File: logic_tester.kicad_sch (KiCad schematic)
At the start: 20 parts, among them U1 LM339D

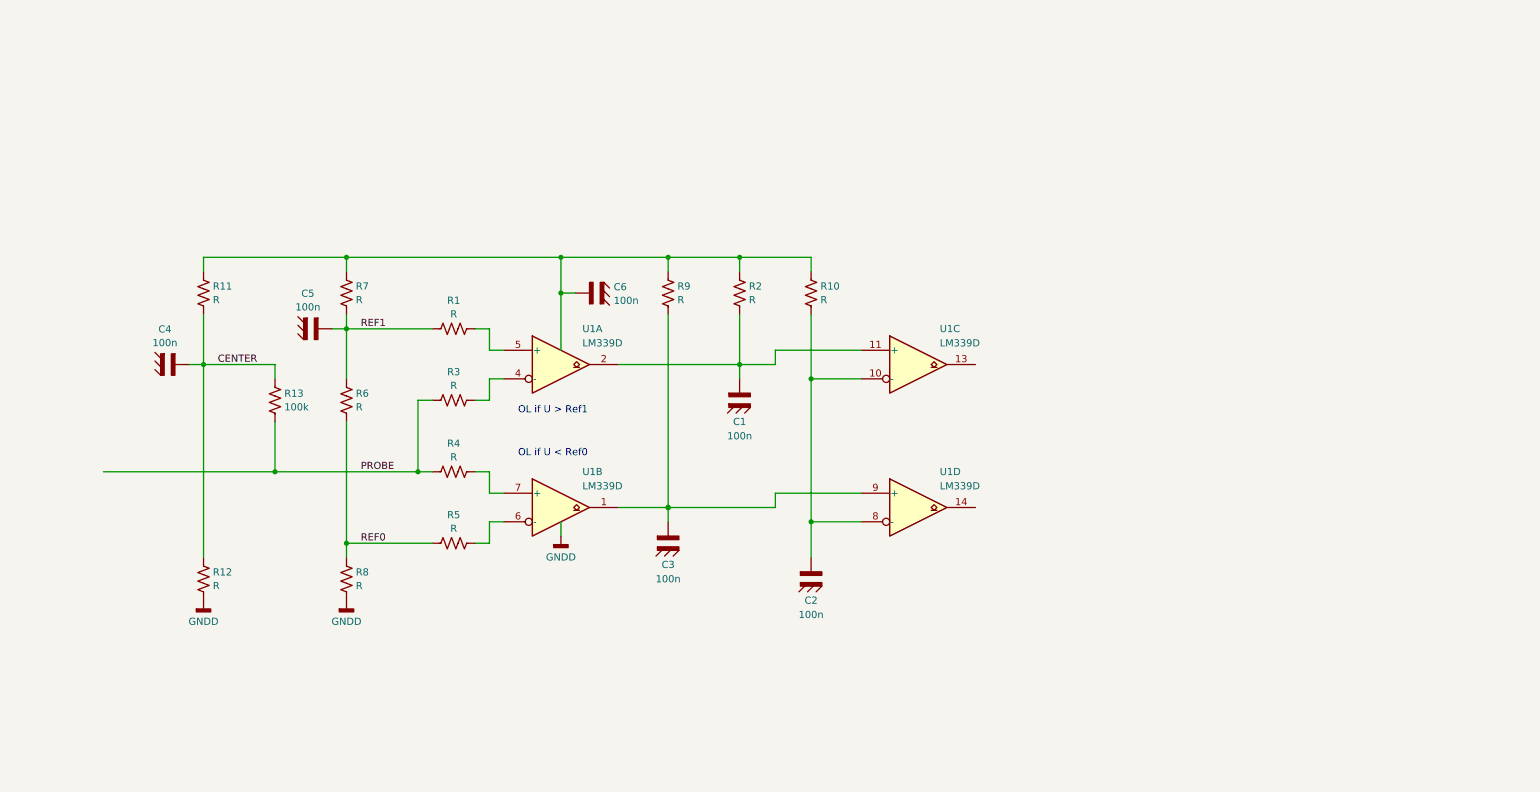
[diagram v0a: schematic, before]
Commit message: Leds with direct supply - bad idea
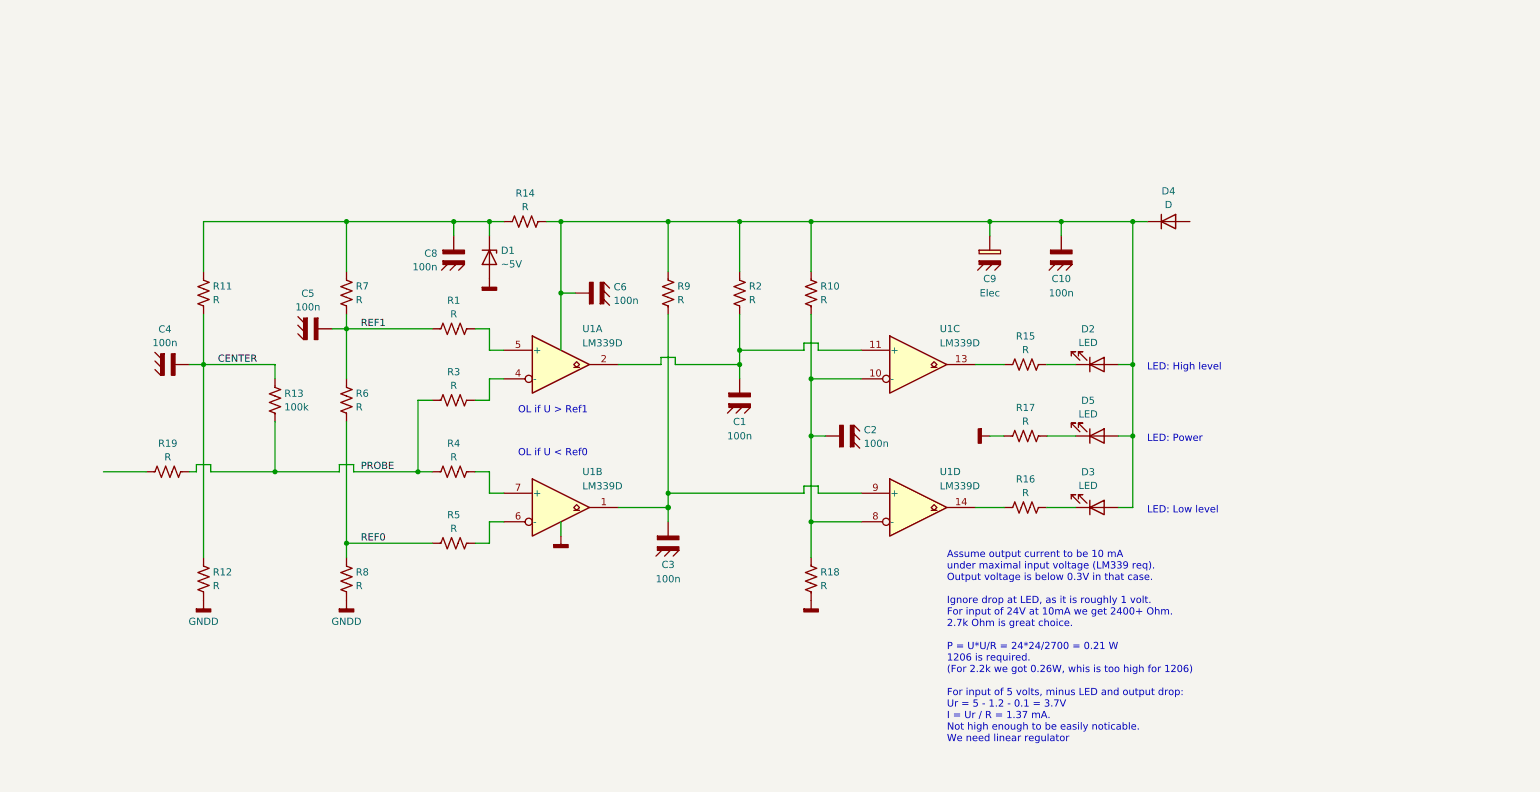
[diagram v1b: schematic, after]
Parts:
- added C10, C8: 100n, symbol symbol:C_GND
- added C9: Elec, symbol symbol:CP_GND
- added D1: ~5V, symbol Device:D_Zener
- added D2, D3, D5: LED, symbol Device:LED
- added D4: D, symbol Device:D
- added R14, R15, R16, R17, R18, R19: R, symbol symbol:R
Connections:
- net GNDD: now also C10.2 (GNDD), C8.2 (GNDD), C9.2 (GNDD), D1.2 (A), R17.1, R18.2
- net PROBE: now also R19.2
- net V+: now also C10.1, C9.1, D2.2 (A), D3.2 (A), D4.1 (K), D5.2 (A), R14.2; no longer R11.1, R7.1
- net at C2.1, R10.2, U1.10 (-)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: now also R18.1
- net at U1.14: now also R16.1
- net at U1.13: now also R15.1
- new net: D5.1 (K), R17.2
- new net: D2.1 (K), R15.2
- new net: D3.1 (K), R16.2
- new net: C8.1, D1.1 (K), R11.1, R14.1, R7.1
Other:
- note added: "Assume output current to be 10 mA under maximal input voltage (LM339 req). Output voltage is below 0.3V in that case. Ignore drop at LED, as it is roughly 1 volt. For input of 24V at 10mA we get 2400+ Ohm. 2.7k Ohm is great choice. P = U*U/R = 24*24/2700 = 0.21 W 1206 is required. (For 2.2k we got 0.26W, whis is too high for 1206) For input of 5 volts, minus LED and output drop: Ur = 5 - 1.2 - 0.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"
- note added: "LED: High level"
- note added: "LED: Low level"
- note added: "LED: Power"

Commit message: Voltage regulator added
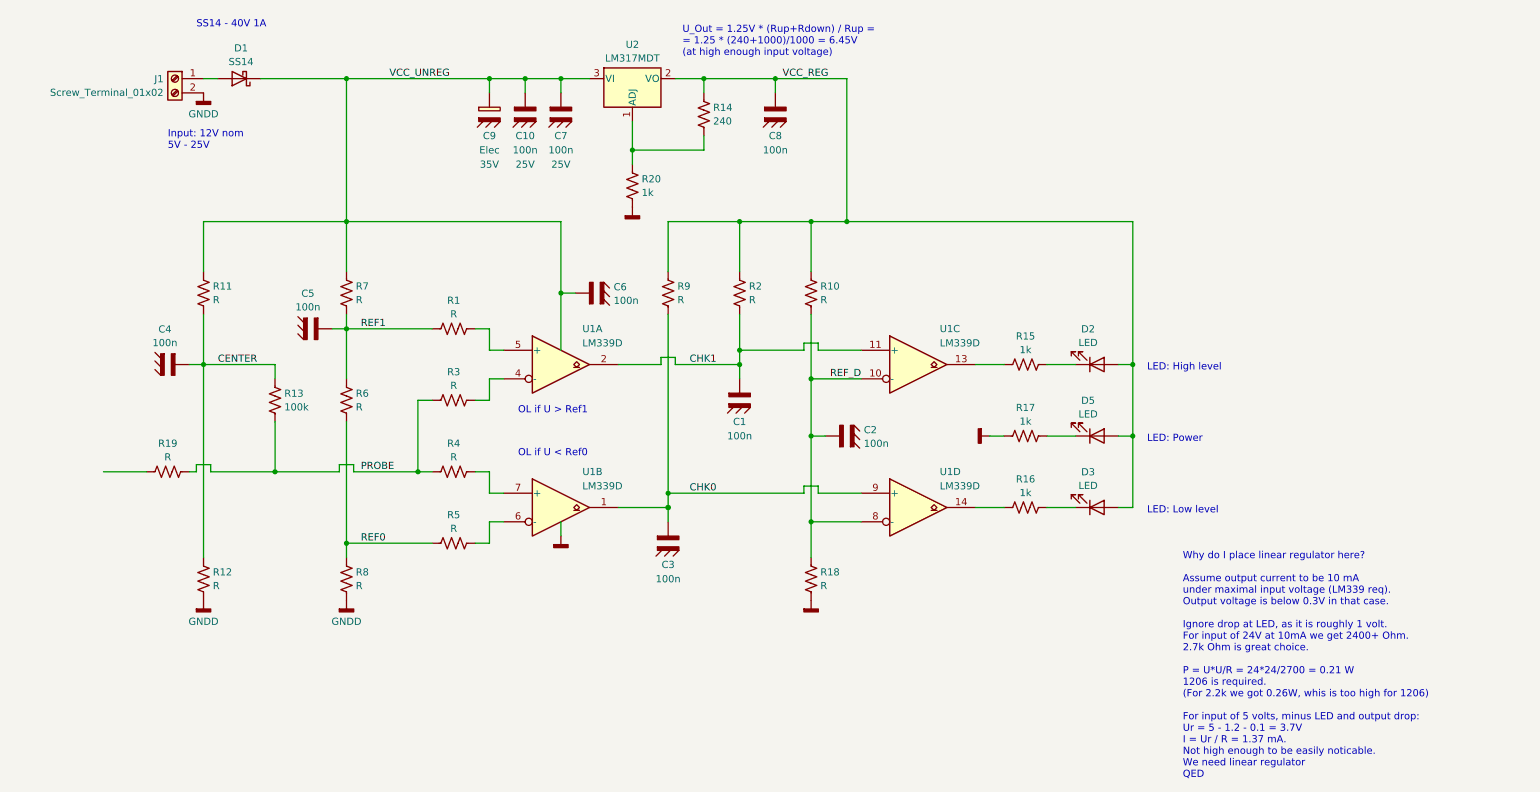
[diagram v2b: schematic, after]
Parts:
- removed D1: ~5V, symbol Device:D_Zener
- removed D4: D, symbol Device:D
- added C7: 100n, symbol symbol:C_GND
- added D1: SS14, symbol Device:D_Schottky
- added J1: Screw_Terminal_01x02, symbol Connector:Screw_Terminal_01x02
- added R20: 1k, symbol symbol:R
- added U2: LM317MDT, NevaDA:D-PAK, symbol symbol:LM317D2P
- C10: Voltage (none) -> 25V
- C9: Voltage (none) -> 35V
- R14: value R -> 240
- R15, R16, R17: value R -> 1k
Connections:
- net GNDD: now also C7.2 (GNDD), J1.2 (Pin_2), R20.2
- net V+: now also R11.1, R7.1, C7.1, D1.1 (K), U2.3 (VI); no longer D2.2 (A), D3.2 (A), D5.2 (A), R10.1, R14.2, R2.1, R9.1
- net CHK0: now reaches C3.1, R9.2, U1.1, U1.9 (+)
- net CHK1: now reaches C1.1, R2.2, U1.11 (+), U1.2
- net REF_D: now reaches C2.1, R10.2, R18.1, U1.10 (-), U1.8 (-)
- net VCC_REG: now reaches C8.1, R14.1
- net VCC_REG: now also D2.2 (A), D3.2 (A), D5.2 (A), R10.1, R2.1, R9.1, U2.2 (VO); no longer R11.1, R7.1
- new net: R14.2, R20.1, U2.1 (ADJ)
- new net: D1.2 (A), J1.1 (Pin_1)
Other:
- note added: "Input: 12V nom 5V - 25V"
- note added: "SS14 - 40V 1A"
- note added: "U_Out = 1.25V * (Rup+Rdown) / Rup = = 1.25 * (240+1000)/1000 = 6.45V (at high enough input voltage)"
- note added: "Why do I place linear regulator here? Assume output current to be 10 mA under maximal input voltage (LM339 req). Output voltage is below 0.3V in that case. Ignore drop at LED, as it is roughly 1 volt. For input of 24V at 10mA we get 2400+ Ohm. 2.7k Ohm is great choice. P = U*U/R = 24*24/2700 = 0.21 W 1206 is required. (For 2.2k we got 0.26W, whis is too high for 1206) For input of 5 volts, minus 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"
- note removed: "Assume output current to be 10 mA under maximal input voltage (LM339 req). Output voltage is below 0.3V in that case. Ignore drop at LED, as it is roughly 1 volt. For input of 24V at 10mA we get 2400+ Ohm. 2.7k Ohm is great choice. P = U*U/R = 24*24/2700 = 0.21 W 1206 is required. (For 2.2k we got 0.26W, whis is too high for 1206) For input of 5 volts, minus LED and output drop: Ur = 5 - 1.2 - 0.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"
- moved on the sheet: C10, C9

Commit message: Capacitors chosen
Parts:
- removed C9: Elec, symbol symbol:CP_GND
- added C9: 22u, NevaDA:C_1206, symbol symbol:C_GND
- C1, C2, C3, C4, C5, C6, C8: footprint (none) -> NevaDA:C_0402; Ceramic (none) -> X7R; Voltage (none) -> 25V
- C10, C7: footprint (none) -> NevaDA:C_0402; Ceramic (none) -> X7R
- J1: value Screw_Terminal_01x02 -> 15EDGR-3.5-02P; footprint (none) -> NevaDA:Terminal_3.5mm_x2
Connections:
- net GNDD: now also C9.2 (GNDD)
- net V+: now also C9.1
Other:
- moved on the sheet: C1

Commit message: Schematics looks OK
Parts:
- removed R19: R, symbol symbol:R
- added J2: Probe, symbol Connector:Conn_01x01_Pin
- D1: footprint (none) -> NevaDA:DO-214AC_SMA
- D2, D3, D5: value LED -> KP-2012MGC; footprint (none) -> NevaDA:LED_KP-2012G
- R1, R3, R4, R5, R6, R7, R8: value R -> 1k; footprint (none) -> NevaDA:R_0603
- R10, R11, R12, R18: value R -> 10k; footprint (none) -> NevaDA:R_0603
- R13: value 100k -> 10k; footprint (none) -> NevaDA:R_0603
- R14, R15, R16, R17, R20: footprint (none) -> NevaDA:R_0603
- R2, R9: value R -> 100k; footprint (none) -> NevaDA:R_0603
- U1: footprint (none) -> NevaDA:SOIC-14
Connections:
- net PROBE: now also J2.1 (Pin_1)
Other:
- note added: "Inputs source about 25uA drop at resistors = 25 mV"
- note added: "tau = R*C = 100k*100n = 10 ms This circuit increases pulse length to make even short pulse noticable"
- moved on the sheet: J1

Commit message: Geo reannotate
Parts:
- renumbered C4 to C1, C2 to C10, C5 to C2, C6 to C3, C9 to C4, C7 to C5, C10 to C6, C3 to C7, C1 to C8, C8 to C9, D5 to D3, D3 to D4, R11 to R1, R4 to R10, R9 to R11, R2 to R12, R14 to R13, R20 to R14, R10 to R15, R18 to R16, R15 to R17, R17 to R18, R16 to R19, R12 to R2, R13 to R3, R6 to R4, R7 to R5, R8 to R6, R1 to R7, R5 to R8, R3 to R9

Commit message: Swap comparators for easier routing
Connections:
- net CHK0: now also U1.11 (+), U1.14; no longer U1.1, U1.9 (+)
- net CHK1: now also U1.1, U1.5 (+); no longer U1.11 (+), U1.2
- net REF_D: now also U1.10 (-), U1.4 (-); no longer U1.10 (-), U1.8 (-)
- net at R8.2: now also U1.8 (-); no longer U1.6 (-)
- net at R10.2: now also U1.9 (+); no longer U1.7 (+)
- net at R19.1: now also U1.13; no longer U1.14
- net at R9.2: now also U1.6 (-); no longer U1.4 (-)
- net at R7.2: now also U1.7 (+); no longer U1.5 (+)
- net at R17.1: now also U1.2; no longer U1.13
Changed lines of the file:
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@@
     )
   )
-  (symbol (lib_id "symbol:LM339") (at 114.3 114.3 0) (unit 2)
+  (symbol (lib_id "symbol:LM339") (at 114.3 114.3 0) (unit 4)
     (in_bom yes) (on_board yes) (dnp no)
     (property "Reference" "U1" (at 118.11 107.95 0) (do_not_autoplace)
@@
       (project "logic_tester"
         (path "/4085a7af-4def-400e-a89c-e37b73aa27bf"
-          (reference "U1") (unit 2)
+          (reference "U1") (unit 4)
         )
       )
@@
     )
   )
-  (symbol (lib_id "symbol:LM339") (at 177.8 114.3 0) (unit 4)
+  (symbol (lib_id "symbol:LM339") (at 177.8 114.3 0) (unit 3)
     (in_bom yes) (on_board yes) (dnp no)
     (property "Reference" "U1" (at 181.61 107.95 0) (do_not_autoplace)
@@
       (project "logic_tester"
         (path "/4085a7af-4def-400e-a89c-e37b73aa27bf"
-          (reference "U1") (unit 4)
+          (reference "U1") (unit 3)
         )
       )
@@
     )
   )
-  (symbol (lib_id "symbol:LM339") (at 177.8 88.9 0) (unit 3)
+  (symbol (lib_id "symbol:LM339") (at 177.8 88.9 0) (unit 1)
     (in_bom yes) (on_board yes) (dnp no)
     (property "Reference" "U1" (at 181.61 82.55 0) (do_not_autoplace)
@@
       (project "logic_tester"
         (path "/4085a7af-4def-400e-a89c-e37b73aa27bf"
-          (reference "U1") (unit 3)
+          (reference "U1") (unit 1)
         )
       )
@@
     )
   )
-  (symbol (lib_id "symbol:LM339") (at 114.3 88.9 0) (unit 1)
+  (symbol (lib_id "symbol:LM339") (at 114.3 88.9 0) (unit 2)
     (in_bom yes) (on_board yes) (dnp no)
     (property "Reference" "U1" (at 118.11 82.55 0) (do_not_autoplace)
@@
       (project "logic_tester"
         (path "/4085a7af-4def-400e-a89c-e37b73aa27bf"
-          (reference "U1") (unit 1)
-        )
-      )
+          (reference "U1") (unit 2)
+        )
+      )

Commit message: Seems fitted
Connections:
- net GNDD: now also J1.1 (Pin_1); no longer J1.2 (Pin_2)
- net at D1.2 (A): now also J1.2 (Pin_2); no longer J1.1 (Pin_1)
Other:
- moved on the sheet: D1, J1
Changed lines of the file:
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@@
     (stroke (width 0) (type default))
   )
-  (wire (pts (xy 43.18 38.1) (xy 53.34 38.1))
+  (wire (pts (xy 43.18 38.1) (xy 59.69 38.1))
     (stroke (width 0) (type default))
   )
@@
     (stroke (width 0) (type default))
   )
-  (wire (pts (xy 60.96 38.1) (xy 76.2 38.1))
+  (wire (pts (xy 67.31 38.1) (xy 76.2 38.1))
     (stroke (width 0) (type default))
   )
@@
     (stroke (width 0) (type default))
   )
-  (text "Input: 12V nom\n5V - 25V" (at 35.56 50.8 0)
-    (effects (font (size 1.27 1.27)) (justify left bottom))
-  )
-  (text "SS14 - 40V 1A" (at 49.53 29.21 0)
+  (text "Input: 12V nom\n5V - 25V" (at 31.75 45.72 0)
+    (effects (font (size 1.27 1.27)) (justify left bottom))
+  )
+  (text "SS14 - 40V 1A" (at 55.88 29.21 0)
     (effects (font (size 1.27 1.27)) (justify left bottom))
   )
@@
     )
   )
-  (symbol (lib_id "Device:D_Schottky") (at 57.15 38.1 180) (unit 1)
-    (in_bom yes) (on_board yes) (dnp no) (fields_autoplaced)
-    (property "Reference" "D1" (at 57.4675 32.6857 0)
-      (effects (font (size 1.27 1.27)))
-    )
-    (property "Value" "SS14" (at 57.4675 35.1099 0)
-      (effects (font (size 1.27 1.27)))
-    )
-    (property "Footprint" "NevaDA:DO-214AC_SMA" (at 57.15 38.1 0)
-      (effects (font (size 1.27 1.27)) hide)
-    )
-    (property "Datasheet" "~" (at 57.15 38.1 0)
+  (symbol (lib_id "Device:D_Schottky") (at 63.5 38.1 180) (unit 1)
+    (in_bom yes) (on_board yes) (dnp no) (fields_autoplaced)
+    (property "Reference" "D1" (at 63.8175 32.6857 0)
+      (effects (font (size 1.27 1.27)))
+    )
+    (property "Value" "SS14" (at 63.8175 35.1099 0)
+      (effects (font (size 1.27 1.27)))
+    )
+    (property "Footprint" "NevaDA:DO-214AC_SMA" (at 63.5 38.1 0)
+      (effects (font (size 1.27 1.27)) hide)
+    )
+    (property "Datasheet" "~" (at 63.5 38.1 0)
       (effects (font (size 1.27 1.27)) hide)
     )
@@
     )
   )
-  (symbol (lib_id "power:GNDD") (at 43.18 40.64 0) (unit 1)
-    (in_bom yes) (on_board yes) (dnp no) (fields_autoplaced)
-    (property "Reference" "#PWR07" (at 43.18 46.99 0)
-      (effects (font (size 1.27 1.27)) hide)
-    )
-    (property "Value" "GNDD" (at 43.18 44.3921 0)
-      (effects (font (size 1.27 1.27)))
-    )
-    (property "Footprint" "" (at 43.18 40.64 0)
-      (effects (font (size 1.27 1.27)) hide)
-    )
-    (property "Datasheet" "" (at 43.18 40.64 0)
+  (symbol (lib_id "power:GNDD") (at 43.18 35.56 90) (unit 1)
+    (in_bom yes) (on_board yes) (dnp no) (fields_autoplaced)
+    (property "Reference" "#PWR07" (at 49.53 35.56 0)
+      (effects (font (size 1.27 1.27)) hide)
+    )
+    (property "Value" "GNDD" (at 45.974 35.56 90)
+      (effects (font (size 1.27 1.27)) (justify right))
+    )
+    (property "Footprint" "" (at 43.18 35.56 0)
+      (effects (font (size 1.27 1.27)) hide)
+    )
+    (property "Datasheet" "" (at 43.18 35.56 0)
       (effects (font (size 1.27 1.27)) hide)
     )
@@
     )
   )
-  (symbol (lib_id "Connector:Screw_Terminal_01x02") (at 38.1 38.1 0) (mirror y) (unit 1)
-    (in_bom yes) (on_board yes) (dnp no) (fields_autoplaced)
-    (property "Reference" "J1" (at 36.068 38.1579 0)
-      (effects (font (size 1.27 1.27)) (justify left))
-    )
-    (property "Value" "15EDGR-3.5-02P" (at 36.068 40.5821 0)
-      (effects (font (size 1.27 1.27)) (justify left))
-    )
-    (property "Footprint" "NevaDA:Terminal_3.5mm_x2" (at 38.1 38.1 0)
-      (effects (font (size 1.27 1.27)) hide)
-    )
-    (property "Datasheet" "~" (at 38.1 38.1 0)
-      (effects (font (size 1.27 1.27)) hide)
-    )
-    (property "Role" "" (at 38.1 38.1 0)
-      (effects (font (size 1.27 1.27)) hide)
-    )
-    (property "Vcc" "" (at 38.1 38.1 0)
-      (effects (font (size 1.27 1.27)))
-    )
-    (property "Voltage" "" (at 38.1 38.1 0)
-      (effects (font (size 1.27 1.27)))
-    )
-    (property "Ceramic" "" (at 38.1 38.1 0)
-      (effects (font (size 1.27 1.27)))
-    )
+  (symbol (lib_id "Connector:Screw_Terminal_01x02") (at 38.1 35.56 0) (mirror y) (unit 1)
+    (in_bom yes) (on_board yes) (dnp no)
+    (property "Reference" "J1" (at 36.068 35.6179 0)
+      (effects (font (size 1.27 1.27)) (justify left))
+    )
+    (property "Value" "15EDGR-3.5-02P" (at 36.068 38.0421 0)
+      (effects (font (size 1.27 1.27)) (justify left))
+    )
+    (property "Footprint" "NevaDA:Terminal_3.5mm_x2" (at 38.1 35.56 0)
+      (effects (font (size 1.27 1.27)) hide)
+    )
+    (property "Datasheet" "~" (at 38.1 35.56 0)
+      (effects (font (size 1.27 1.27)) hide)
+    )
+    (property "Role" "" (at 38.1 35.56 0)
+      (effects (font (size 1.27 1.27)) hide)
+    )
+    (property "Vcc" "" (at 38.1 35.56 0)
+      (effects (font (size 1.27 1.27)))
+    )
+    (property "Voltage" "" (at 38.1 35.56 0)
+      (effects (font (size 1.27 1.27)))
+    )
+    (property "Ceramic" "" (at 38.1 35.56 0)
+      (effects (font (size 1.27 1.27)))
+    )

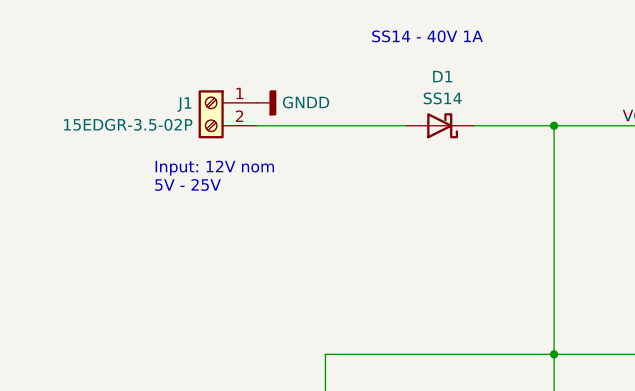
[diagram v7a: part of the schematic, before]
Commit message: Probe pad added
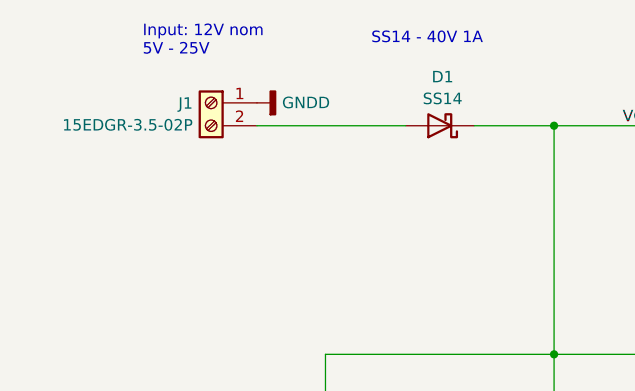
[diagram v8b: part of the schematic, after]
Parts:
- J2: footprint (none) -> NevaDA:Pad_Wire
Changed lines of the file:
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@@
     (stroke (width 0) (type default))
   )
-  (text "Input: 12V nom\n5V - 25V" (at 31.75 45.72 0)
+  (text "Input: 12V nom\n5V - 25V" (at 30.48 30.48 0)
     (effects (font (size 1.27 1.27)) (justify left bottom))
   )
@@
       (effects (font (size 1.27 1.27)) (justify right))
     )
-    (property "Footprint" "" (at 36.83 107.95 0)
-      (effects (font (size 1.27 1.27)) hide)
-    )
+    (property "Footprint" "NevaDA:Pad_Wire" (at 36.83 107.95 0)
+      (effects (font (size 1.27 1.27)) hide)
+    )
